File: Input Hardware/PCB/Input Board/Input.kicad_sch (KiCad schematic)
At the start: 4 parts

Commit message: Update Input.kicad_sch
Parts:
- removed SW?: RotaryEncoder_Switch_MP, Rotary_Encoder:RotaryEncoder_Alps_EC11E-Switch_Vertical_H20mm, symbol Device:RotaryEncoder_Switch_MP
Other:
- note added: "Zoom"
- note added: "x-pan"
- note added: "y-pan"
- moved on the sheet: SW?
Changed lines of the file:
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@@
 	(generator_version "9.0")
 	(paper "A4")
+	(text "x-pan\n"
+		(exclude_from_sim no)
+		(at 107.95 31.75 0)
+		(effects
+			(font
+				(size 1.27 1.27)
+			)
+		)
+	)
+	(text "y-pan\n"
+		(exclude_from_sim no)
+		(at 134.62 31.75 0)
+		(effects
+			(font
+				(size 1.27 1.27)
+			)
+		)
+	)
+	(text "Zoom\n"
+		(exclude_from_sim no)
+		(at 81.28 31.75 0)
+		(effects
+			(font
+				(size 1.27 1.27)
+			)
+		)
+	)
 	(symbol
 		(lib_id "Device:RotaryEncoder_Switch_MP")
-		(at 57.15 44.45 0)
+		(at 81.28 45.72 0)
 		(unit 1)
 		(exclude_from_sim no)
@@
 		(fields_autoplaced yes)
 		(property "Reference" "SW?"
-			(at 57.15 34.29 0)
+			(at 81.28 35.56 0)
 			(effects
 				(font
@@
 		)
 		(property "Value" "RotaryEncoder_Switch_MP"
-			(at 57.15 36.83 0)
+			(at 81.28 38.1 0)
 			(effects
 				(font
@@
 		)
 		(property "Footprint" "Rotary_Encoder:RotaryEncoder_Alps_EC11E-Switch_Vertical_H20mm"
-			(at 53.34 40.386 0)
+			(at 77.47 41.656 0)
 			(effects
 				(font
@@
 		)
 		(property "Datasheet" "~"
-			(at 57.15 57.15 0)
+			(at 81.28 58.42 0)
 			(effects
 				(font
@@
 		)
 		(property "Description" "Rotary encoder, dual channel, incremental quadrate outputs, with switch and MP Pin"
-			(at 57.15 59.69 0)
+			(at 81.28 60.96 0)
 			(effects
 				(font
@@
 	(symbol
 		(lib_id "Device:RotaryEncoder_Switch_MP")
-		(at 58.42 83.82 0)
+		(at 134.62 45.72 0)
 		(unit 1)
 		(exclude_from_sim no)
@@
 		(fields_autoplaced yes)
 		(property "Reference" "SW?"
-			(at 58.42 73.66 0)
+			(at 134.62 35.56 0)
 			(effects
 				(font
@@
 		)
 		(property "Value" "RotaryEncoder_Switch_MP"
-			(at 58.42 76.2 0)
+			(at 134.62 38.1 0)
 			(effects
 				(font
@@
 		)
 		(property "Footprint" "Rotary_Encoder:RotaryEncoder_Alps_EC11E-Switch_Vertical_H20mm"
-			(at 54.61 79.756 0)
+			(at 130.81 41.656 0)
 			(effects
 				(font
@@
 		)
 		(property "Datasheet" "~"
-			(at 58.42 96.52 0)
+			(at 134.62 58.42 0)
 			(effects
 				(font
@@
 		)
 		(property "Description" "Rotary encoder, dual channel, incremental quadrate outputs, with switch and MP Pin"
-			(at 58.42 99.06 0)
-			(effects
-				(font
-					(size 1.27 1.27)
-				)
-				(hide yes)
-			)
-		)
-		(pin "S2"
-		)
-		(pin "C"
-		)
-		(pin "MP"
-		)
-		(pin "B"
-		)
-		(pin "A"
-		)
-		(pin "S1"
-		)
-		(instances
-			(project "Input Board"
-				(path "/198ad8d1-66e3-4deb-889c-1af2b81e67c3/6ff1d53f-9520-4015-acff-de10540e78ee"
-					(reference "SW?")
-					(unit 1)
-				)
-			)
-		)
-	)
-	(symbol
-		(lib_id "Device:RotaryEncoder_Switch_MP")
-		(at 107.95 83.82 0)
-		(unit 1)
-		(exclude_from_sim no)
-		(in_bom yes)
-		(on_board yes)
-		(dnp no)
-		(fields_autoplaced yes)
-		(property "Reference" "SW?"
-			(at 107.95 73.66 0)
-			(effects
-				(font
-					(size 1.27 1.27)
-				)
-			)
-		)
-		(property "Value" "RotaryEncoder_Switch_MP"
-			(at 107.95 76.2 0)
-			(effects
-				(font
-					(size 1.27 1.27)
-				)
-			)
-		)
-		(property "Footprint" "Rotary_Encoder:RotaryEncoder_Alps_EC11E-Switch_Vertical_H20mm"
-			(at 104.14 79.756 0)
-			(effects
-				(font
-					(size 1.27 1.27)
-				)
-				(hide yes)
-			)
-		)
-		(property "Datasheet" "~"
-			(at 107.95 96.52 0)
-			(effects
-				(font
-					(size 1.27 1.27)
-				)
-				(hide yes)
-			)
-		)
-		(property "Description" "Rotary encoder, dual channel, incremental quadrate outputs, with switch and MP Pin"
-			(at 107.95 99.06 0)
-			(effects
-				(font
+			(at 134.62 60.96 0)
+			(effects
+				(font

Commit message: more fixes
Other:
- note added: "D-Pad? Gain? Transform Selector (z, laplace, fourier)?"
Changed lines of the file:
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@@
+		)
+	)
+	(text "D-Pad?\nGain?\nTransform  Selector (z, laplace, fourier)?\n\n"
+		(exclude_from_sim no)
+		(at 177.8 31.75 0)
+		(effects
+			(font
+				(size 1.27 1.27)
+			)
 		)
 	)

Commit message: spices
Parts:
- added SW? (x2): RotaryEncoder_Switch_MP, Rotary_Encoder:RotaryEncoder_Alps_EC11E-Switch_Vertical_H20mm, symbol Device:RotaryEncoder_Switch_MP
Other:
- note added: "D-Pad"
- note added: "Gain"
- note added: "Transform Selector"
- note removed: "D-Pad? Gain? Transform Selector (z, laplace, fourier)?"
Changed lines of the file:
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@@
+		)
+	)
+	(text "Gain"
+		(exclude_from_sim no)
+		(at 161.29 31.75 0)
+		(effects
+			(font
+				(size 1.27 1.27)
+			)
 		)
 	)
@@
 		)
 	)
-	(text "D-Pad?\nGain?\nTransform  Selector (z, laplace, fourier)?\n\n"
+	(text "Transform Selector"
 		(exclude_from_sim no)
-		(at 177.8 31.75 0)
+		(at 187.96 31.75 0)
 		(effects
 			(font
@@
 			)
 		)
+	)
+	(text "D-Pad"
+		(exclude_from_sim no)
+		(at 222.25 44.45 0)
+		(effects
+			(font
+				(size 1.27 1.27)
+			)
+		)
+	)
+	(symbol
+		(lib_id "Device:RotaryEncoder_Switch_MP")
+		(at 161.29 45.72 0)
+		(unit 1)
+		(exclude_from_sim no)
+		(in_bom yes)
+		(on_board yes)
+		(dnp no)
+		(fields_autoplaced yes)
+		(property "Reference" "SW?"
+			(at 161.29 35.56 0)
+			(effects
+				(font
+					(size 1.27 1.27)
+				)
+			)
+		)
+		(property "Value" "RotaryEncoder_Switch_MP"
+			(at 161.29 38.1 0)
+			(effects
+				(font
+					(size 1.27 1.27)
+				)
+			)
+		)
+		(property "Footprint" "Rotary_Encoder:RotaryEncoder_Alps_EC11E-Switch_Vertical_H20mm"
+			(at 157.48 41.656 0)
+			(effects
+				(font
+					(size 1.27 1.27)
+				)
+				(hide yes)
+			)
+		)
+		(property "Datasheet" "~"
+			(at 161.29 58.42 0)
+			(effects
+				(font
+					(size 1.27 1.27)
+				)
+				(hide yes)
+			)
+		)
+		(property "Description" "Rotary encoder, dual channel, incremental quadrate outputs, with switch and MP Pin"
+			(at 161.29 60.96 0)
+			(effects
+				(font
+					(size 1.27 1.27)
+				)
+				(hide yes)
+			)
+		)
+		(pin "S2"
+		)
+		(pin "C"
+		)
+		(pin "MP"
+		)
+		(pin "B"
+		)
+		(pin "A"
+		)
+		(pin "S1"
+		)
+		(instances
+			(project "Input Board"
+				(path "/198ad8d1-66e3-4deb-889c-1af2b81e67c3/6ff1d53f-9520-4015-acff-de10540e78ee"
+					(reference "SW?")
+					(unit 1)
+				)
+			)
+		)
+	)
+	(symbol
+		(lib_id "Device:RotaryEncoder_Switch_MP")
+		(at 187.96 45.72 0)
+		(unit 1)
+		(exclude_from_sim no)
+		(in_bom yes)
+		(on_board yes)
+		(dnp no)
+		(fields_autoplaced yes)
+		(property "Reference" "SW?"
+			(at 187.96 35.56 0)
+			(effects
+				(font
+					(size 1.27 1.27)
+				)
+			)
+		)
+		(property "Value" "RotaryEncoder_Switch_MP"
+			(at 187.96 38.1 0)
+			(effects
+				(font
+					(size 1.27 1.27)
+				)
+			)
+		)
+		(property "Footprint" "Rotary_Encoder:RotaryEncoder_Alps_EC11E-Switch_Vertical_H20mm"
+			(at 184.15 41.656 0)
+			(effects
+				(font
+					(size 1.27 1.27)
+				)
+				(hide yes)
+			)
+		)
+		(property "Datasheet" "~"
+			(at 187.96 58.42 0)
+			(effects
+				(font
+					(size 1.27 1.27)
+				)
+				(hide yes)
+			)
+		)
+		(property "Description" "Rotary encoder, dual channel, incremental quadrate outputs, with switch and MP Pin"
+			(at 187.96 60.96 0)
+			(effects
+				(font
+					(size 1.27 1.27)
+				)
+				(hide yes)
+			)
+		)
+		(pin "S2"
+		)
+		(pin "C"
+		)
+		(pin "MP"
+		)
+		(pin "B"
+		)
+		(pin "A"
+		)
+		(pin "S1"
+		)
+		(instances
+			(project "Input Board"
+				(path "/198ad8d1-66e3-4deb-889c-1af2b81e67c3/6ff1d53f-9520-4015-acff-de10540e78ee"
+					(reference "SW?")
+					(unit 1)
+				)
+			)
+		)

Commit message: help
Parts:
- removed SW? (x5): RotaryEncoder_Switch_MP, Rotary_Encoder:RotaryEncoder_Alps_EC11E-Switch_Vertical_H20mm, symbol Device:RotaryEncoder_Switch_MP
- added S? (x2): TS12-74-60, TS12-74-60:TS127460, symbol TS12-74-60:TS12-74-60
- added SW? (x2): Rotary encoder, Connector_PinHeader_2.54mm:PinHeader_1x05_P2.54mm_Vertical_SMD_Pin1Right, symbol Connector_Generic:Conn_01x05
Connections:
- new net GND: S?.MP1, S?.MP1, S?.MP2, S?.MP2
- new net I_COM: S?.2 (COM), SW?.1 (Pin_1)
- new net O_CENTER: S?.5 (NO), S?.5 (NO)
- new net O_COM: S?.2 (COM), SW?.1 (Pin_1)
- new net O_DOWN: S?.4 (F5), S?.4 (F5)
- new net O_LEFT: S?.3 (F4), S?.3 (F4)
- new net O_RIGHT: S?.6 (F3), S?.6 (F3)
- new net O_UP: S?.1 (F2), S?.1 (F2)
- new net S_A: SW?.5 (Pin_5), SW?.5 (Pin_5)
- new net S_B: SW?.4 (Pin_4), SW?.4 (Pin_4)
- new net S_PUSH: SW?.3 (Pin_3), SW?.3 (Pin_3)
- no-connect marks 0 -> 2
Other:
- note added: "Input offset"
- note added: "Input scale"
- note added: "Output offset"
- note added: "Output scale"
- note added: "TBD"
- note added: "X/Y"
- note removed: "D-Pad"
- note removed: "Gain"
- note removed: "Transform Selector"
- note removed: "Zoom"
- note removed: "x-pan"
- note removed: "y-pan"

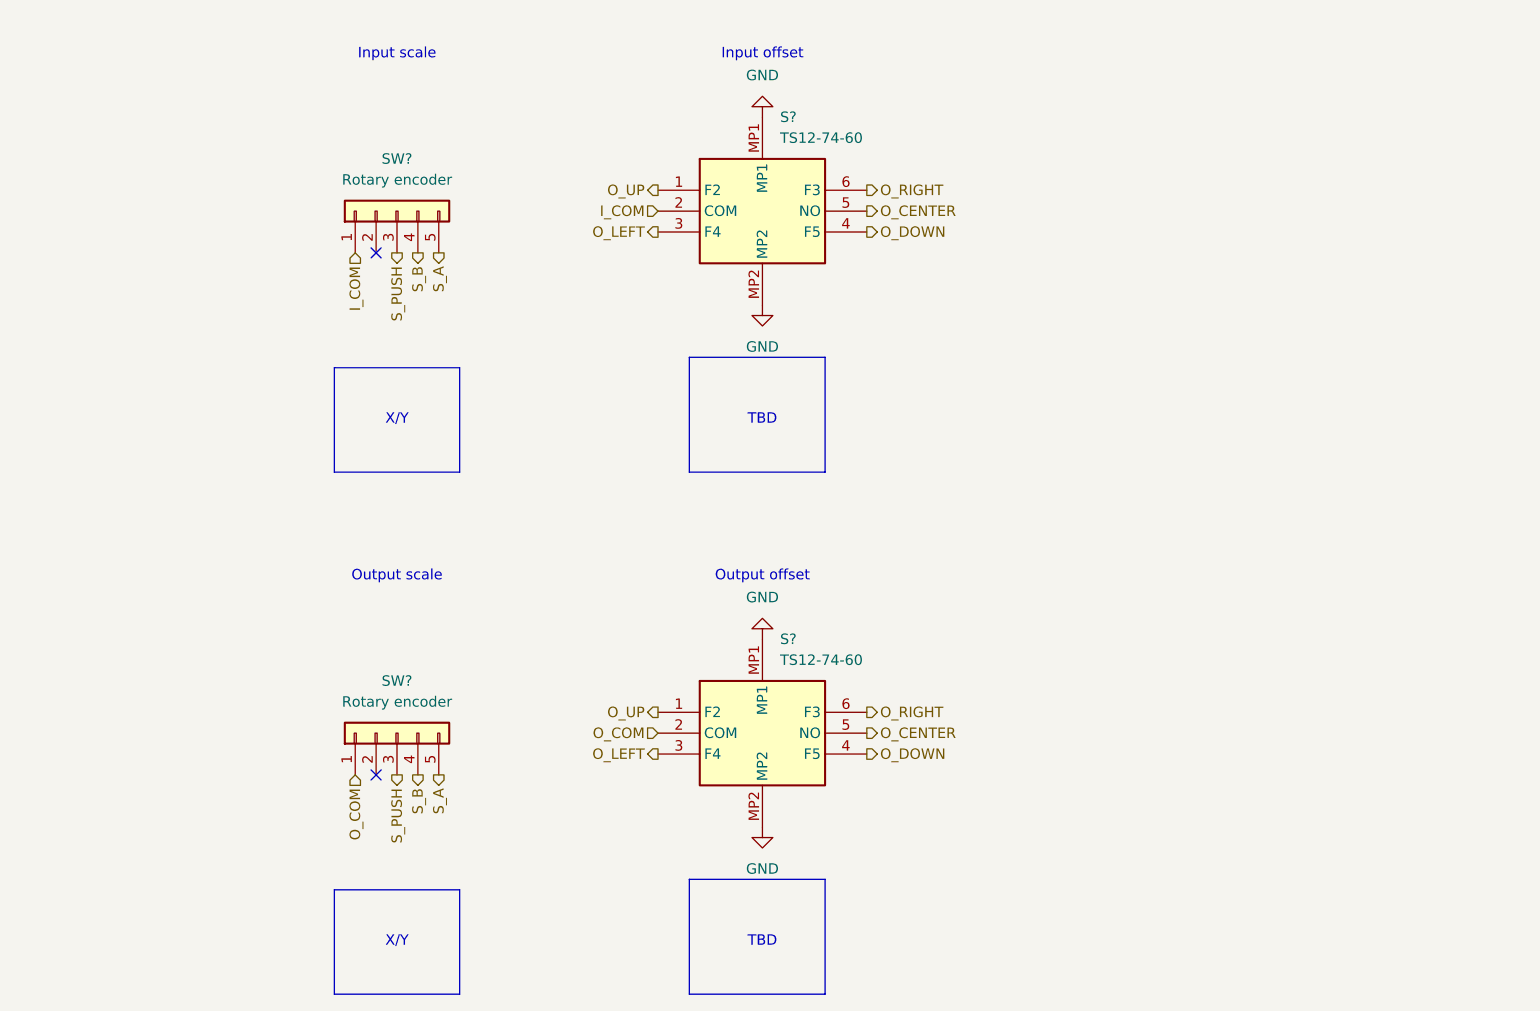
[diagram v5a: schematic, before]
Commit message: kicad fix
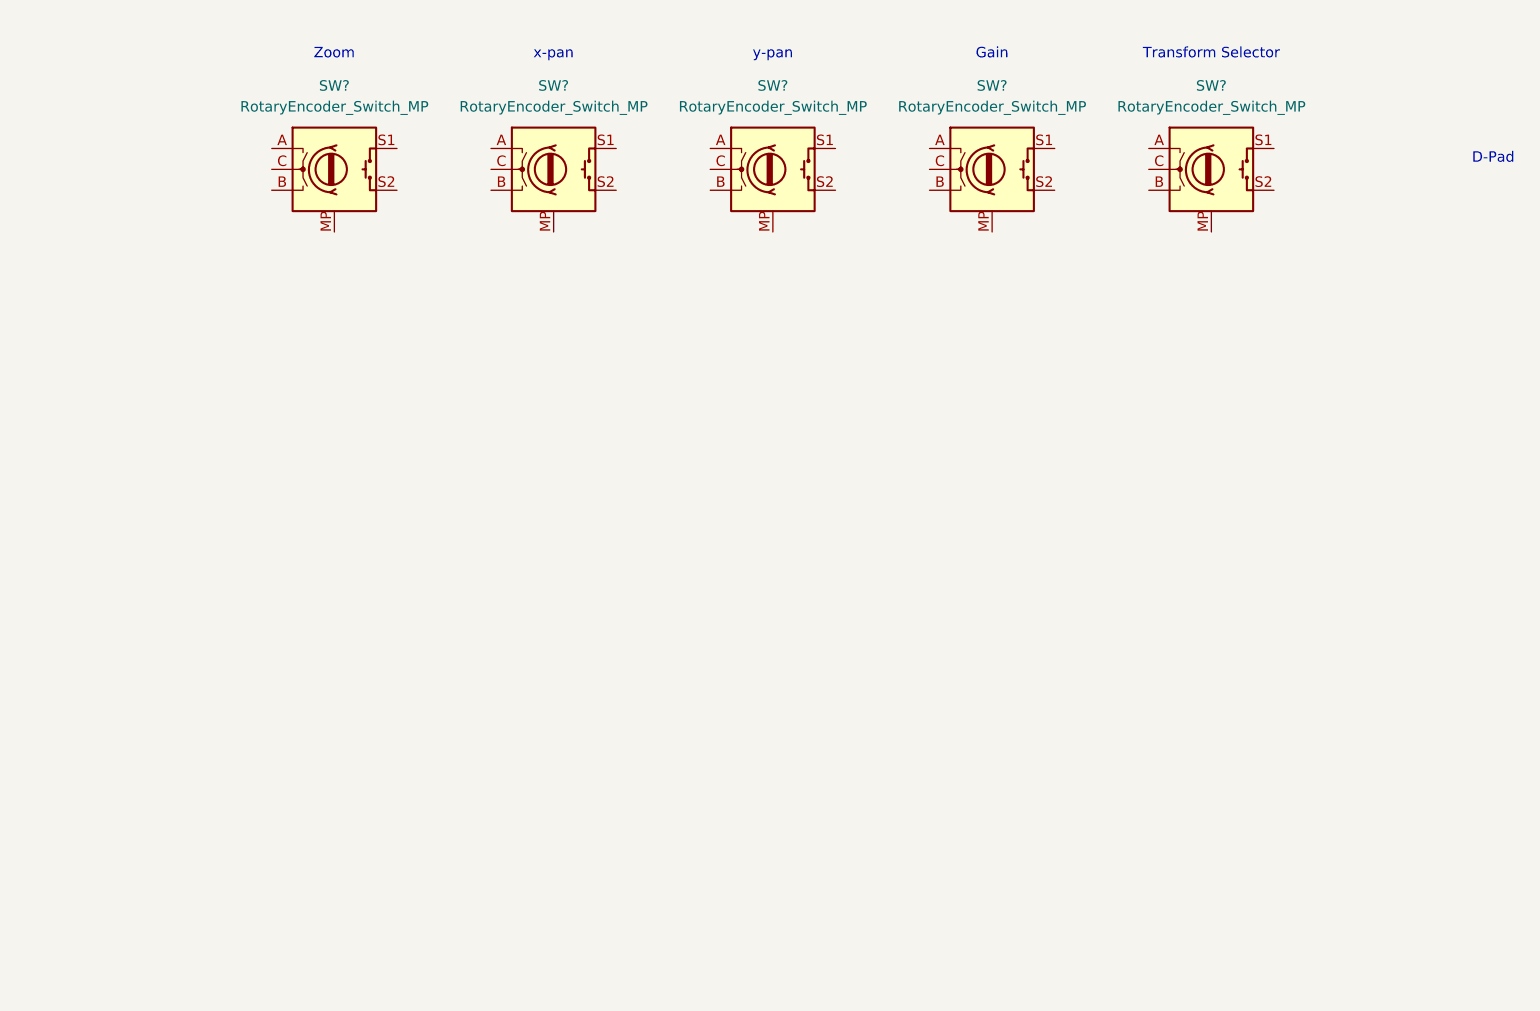
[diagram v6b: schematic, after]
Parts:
- removed S? (x2): TS12-74-60, TS12-74-60:TS127460, symbol TS12-74-60:TS12-74-60
- removed SW? (x2): Rotary encoder, Connector_PinHeader_2.54mm:PinHeader_1x05_P2.54mm_Vertical_SMD_Pin1Right, symbol Connector_Generic:Conn_01x05
- added SW? (x5): RotaryEncoder_Switch_MP, Rotary_Encoder:RotaryEncoder_Alps_EC11E-Switch_Vertical_H20mm, symbol Device:RotaryEncoder_Switch_MP
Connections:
- no-connect marks 2 -> 0
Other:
- note added: "D-Pad"
- note added: "Gain"
- note added: "Transform Selector"
- note added: "Zoom"
- note added: "x-pan"
- note added: "y-pan"
- note removed: "Input offset"
- note removed: "Input scale"
- note removed: "Output offset"
- note removed: "Output scale"
- note removed: "TBD"
- note removed: "X/Y"
